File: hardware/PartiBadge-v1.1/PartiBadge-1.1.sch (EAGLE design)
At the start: 23 parts, among them J1 I2C, J2 Supply

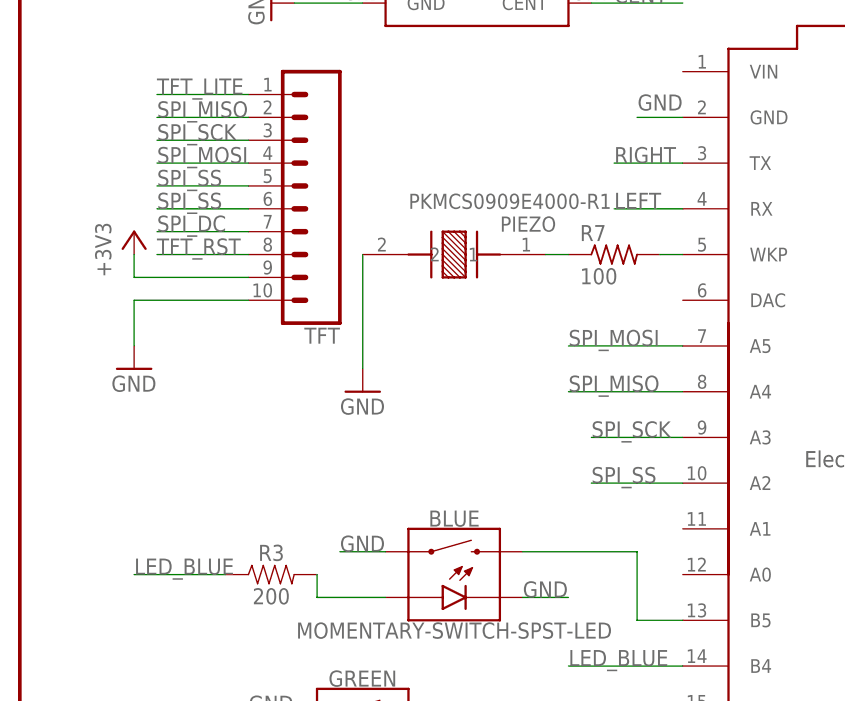
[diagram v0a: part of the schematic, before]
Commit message: moved tft cs pin; closes #50
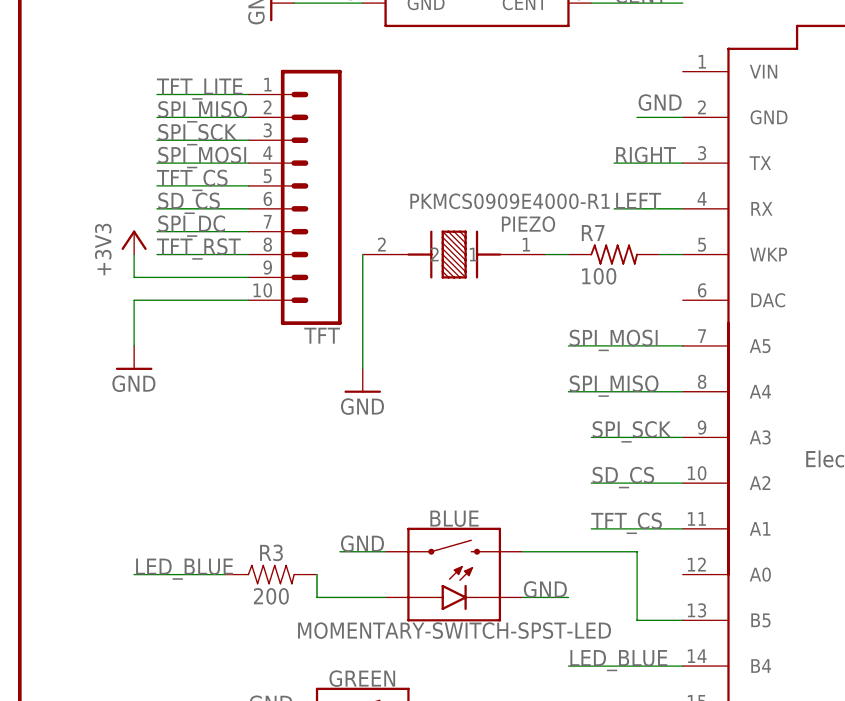
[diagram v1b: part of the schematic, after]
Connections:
- removed net SPI_SS: ELECTRON.A2, TFT.5, TFT.6
- new net SD_CS: ELECTRON.A2, TFT.6
- new net TFT_CS: ELECTRON.A1, TFT.5
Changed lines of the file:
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@@
 </segment>
 </net>
-<net name="SPI_SS" class="0">
+<net name="SD_CS" class="0">
 <segment>
 <pinref part="ELECTRON" gate="G$1" pin="A2"/>
 <wire x1="12.7" y1="48.26" x2="2.54" y2="48.26" width="0.1524" layer="91"/>
 <label x="2.54" y="48.26" size="1.778" layer="95"/>
-</segment>
-<segment>
-<pinref part="TFT" gate="G$1" pin="5"/>
-<wire x1="-35.56" y1="81.28" x2="-45.72" y2="81.28" width="0.1524" layer="91"/>
-<label x="-45.72" y="81.28" size="1.778" layer="95"/>
 </segment>
 <segment>
@@
 </segment>
 </net>
+<net name="TFT_CS" class="0">
+<segment>
+<pinref part="TFT" gate="G$1" pin="5"/>
+<wire x1="-35.56" y1="81.28" x2="-45.72" y2="81.28" width="0.1524" layer="91"/>
+<label x="-45.72" y="81.28" size="1.778" layer="95"/>
+</segment>
+<segment>
+<pinref part="ELECTRON" gate="G$1" pin="A1"/>
+<wire x1="12.7" y1="43.18" x2="2.54" y2="43.18" width="0.1524" layer="91"/>
+<label x="2.54" y="43.18" size="1.778" layer="95"/>
+</segment>
+</net>

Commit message: rev partibadge hardware for ndc oslo
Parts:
- added ETHANOL: (no value), SparkFun-Connectors:CONN_08"
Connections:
- new net RX: ELECTRON.RX, ETHANOL.2
- new net TX: ELECTRON.TX, ETHANOL.3
- net 3V3: now also ETHANOL.8
- net GND: now also ETHANOL.6
- net LEFT: now also ELECTRON.DAC; no longer ELECTRON.RX
- net RIGHT: now also ELECTRON.A0; no longer ELECTRON.TX
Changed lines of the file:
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@@
 </part>
 <part name="R8" library="rcl" library_urn="urn:adsk.eagle:library:334" deviceset="R-US_" device="M0805" package3d_urn="urn:adsk.eagle:package:23556/1" value="100"/>
+<part name="ETHANOL" library="SparkFun-Connectors" library_urn="urn:adsk.eagle:library:513" deviceset="CONN_08" device="&quot;" package3d_urn="urn:adsk.eagle:package:38138/1"/>
+<part name="GND7" library="supply1" library_urn="urn:adsk.eagle:library:371" deviceset="GND" device=""/>
+<part name="+3V7" library="supply1" library_urn="urn:adsk.eagle:library:371" deviceset="+3V3" device=""/>
 </parts>
 <sheets>
@@
 <instance part="PIEZO" gate="G$1" x="-12.7" y="73.66" smashed="yes" rot="R270">
 <attribute name="NAME" x="-7.601059375" y="76.2" size="1.68265" layer="95"/>
-<attribute name="VALUE" x="-17.769109375" y="78.734559375" size="1.679990625" layer="96"/>
+<attribute name="VALUE" x="-22.849109375" y="68.574559375" size="1.679990625" layer="96"/>
 </instance>
 <instance part="S5" gate="1" x="58.42" y="15.24" rot="R180"/>
@@
 <instance part="PARTIFRAME" gate="V" x="86.36" y="-40.64"/>
 <instance part="R8" gate="G$1" x="78.74" y="20.32" rot="R90"/>
+<instance part="ETHANOL" gate="G$1" x="53.34" y="-12.7" rot="R180"/>
+<instance part="GND7" gate="1" x="40.64" y="-17.78" rot="R270"/>
+<instance part="+3V7" gate="G$1" x="40.64" y="-22.86" rot="R90"/>
 </instances>
 <busses>
@@
 <pinref part="GND6" gate="1" pin="GND"/>
 <wire x1="-22.86" y1="101.6" x2="-30.48" y2="101.6" width="0.1524" layer="91"/>
+</segment>
+<segment>
+<pinref part="ETHANOL" gate="G$1" pin="6"/>
+<wire x1="48.26" y1="-17.78" x2="43.18" y2="-17.78" width="0.1524" layer="91"/>
+<pinref part="GND7" gate="1" pin="GND"/>
 </segment>
 </net>
@@
 <wire x1="78.74" y1="25.4" x2="78.74" y2="30.48" width="0.1524" layer="91"/>
 </segment>
+<segment>
+<pinref part="ETHANOL" gate="G$1" pin="8"/>
+<wire x1="48.26" y1="-22.86" x2="43.18" y2="-22.86" width="0.1524" layer="91"/>
+<pinref part="+3V7" gate="G$1" pin="+3V3"/>
+</segment>
 </net>
 <net name="N$4" class="0">
@@
 <segment>
 <pinref part="BLUE" gate="G$1" pin="2"/>
-<wire x1="-5.08" y1="40.64" x2="7.62" y2="40.64" width="0.1524" layer="91"/>
-<wire x1="7.62" y1="40.64" x2="7.62" y2="33.02" width="0.1524" layer="91"/>
+<wire x1="-5.08" y1="40.64" x2="2.54" y2="40.64" width="0.1524" layer="91"/>
+<wire x1="2.54" y1="40.64" x2="2.54" y2="33.02" width="0.1524" layer="91"/>
 <pinref part="ELECTRON" gate="G$1" pin="B5"/>
-<wire x1="7.62" y1="33.02" x2="12.7" y2="33.02" width="0.1524" layer="91"/>
+<wire x1="2.54" y1="33.02" x2="12.7" y2="33.02" width="0.1524" layer="91"/>
 </segment>
 </net>
@@
 </segment>
 <segment>
-<pinref part="ELECTRON" gate="G$1" pin="RX"/>
-<wire x1="12.7" y1="78.74" x2="5.08" y2="78.74" width="0.1524" layer="91"/>
-<label x="5.08" y="78.74" size="1.778" layer="95"/>
+<pinref part="ELECTRON" gate="G$1" pin="DAC"/>
+<wire x1="12.7" y1="68.58" x2="7.62" y2="68.58" width="0.1524" layer="91"/>
+<label x="7.62" y="68.58" size="1.778" layer="95"/>
 </segment>
 </net>
@@
 </segment>
 <segment>
-<pinref part="ELECTRON" gate="G$1" pin="TX"/>
-<wire x1="12.7" y1="83.82" x2="5.08" y2="83.82" width="0.1524" layer="91"/>
-<label x="5.08" y="83.82" size="1.778" layer="95"/>
+<pinref part="ELECTRON" gate="G$1" pin="A0"/>
+<wire x1="12.7" y1="38.1" x2="5.08" y2="38.1" width="0.1524" layer="91"/>
+<label x="5.08" y="38.1" size="1.778" layer="95"/>
 </segment>
 </net>
@@
 </segment>
 </net>
+<net name="RX" class="0">
+<segment>
+<pinref part="ETHANOL" gate="G$1" pin="2"/>
+<wire x1="48.26" y1="-7.62" x2="43.18" y2="-7.62" width="0.1524" layer="91"/>
+<label x="43.18" y="-7.62" size="1.778" layer="95"/>
+</segment>
+<segment>
+<pinref part="ELECTRON" gate="G$1" pin="RX"/>
+<wire x1="12.7" y1="78.74" x2="7.62" y2="78.74" width="0.1524" layer="91"/>
+<label x="7.62" y="78.74" size="1.778" layer="95"/>
+</segment>
+</net>
+<net name="TX" class="0">
+<segment>
+<pinref part="ETHANOL" gate="G$1" pin="3"/>
+<wire x1="48.26" y1="-10.16" x2="43.18" y2="-10.16" width="0.1524" layer="91"/>
+<label x="43.18" y="-10.16" size="1.778" layer="95"/>
+</segment>
+<segment>
+<pinref part="ELECTRON" gate="G$1" pin="TX"/>
+<wire x1="12.7" y1="83.82" x2="7.62" y2="83.82" width="0.1524" layer="91"/>
+<label x="7.62" y="83.82" size="1.778" layer="95"/>
+</segment>
+</net>

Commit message: updated schematic and board
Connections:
- removed net RX: ELECTRON.RX, ETHANOL.2
- removed net TX: ELECTRON.TX, ETHANOL.3
- new net ELECTRON_RX: ELECTRON.RX, ETHANOL.3
- new net ELECTRON_TX: ELECTRON.TX, ETHANOL.2
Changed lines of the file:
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@@
 </segment>
 </net>
-<net name="RX" class="0">
+<net name="ELECTRON_RX" class="0">
+<segment>
+<pinref part="ELECTRON" gate="G$1" pin="RX"/>
+<wire x1="12.7" y1="78.74" x2="-5.08" y2="78.74" width="0.1524" layer="91"/>
+<label x="-5.08" y="78.74" size="1.778" layer="95"/>
+</segment>
+<segment>
+<pinref part="ETHANOL" gate="G$1" pin="3"/>
+<wire x1="48.26" y1="-10.16" x2="30.48" y2="-10.16" width="0.1524" layer="91"/>
+<label x="30.48" y="-10.16" size="1.778" layer="95"/>
+</segment>
+</net>
+<net name="ELECTRON_TX" class="0">
+<segment>
+<pinref part="ELECTRON" gate="G$1" pin="TX"/>
+<wire x1="12.7" y1="83.82" x2="-5.08" y2="83.82" width="0.1524" layer="91"/>
+<label x="-5.08" y="83.82" size="1.778" layer="95"/>
+</segment>
 <segment>
 <pinref part="ETHANOL" gate="G$1" pin="2"/>
-<wire x1="48.26" y1="-7.62" x2="43.18" y2="-7.62" width="0.1524" layer="91"/>
-<label x="43.18" y="-7.62" size="1.778" layer="95"/>
-</segment>
-<segment>
-<pinref part="ELECTRON" gate="G$1" pin="RX"/>
-<wire x1="12.7" y1="78.74" x2="7.62" y2="78.74" width="0.1524" layer="91"/>
-<label x="7.62" y="78.74" size="1.778" layer="95"/>
+<wire x1="48.26" y1="-7.62" x2="30.48" y2="-7.62" width="0.1524" layer="91"/>
+<label x="30.48" y="-7.62" size="1.778" layer="95"/>
 </segment>
 </net>
-<net name="TX" class="0">
-<segment>
-<pinref part="ETHANOL" gate="G$1" pin="3"/>
-<wire x1="48.26" y1="-10.16" x2="43.18" y2="-10.16" width="0.1524" layer="91"/>
-<label x="43.18" y="-10.16" size="1.778" layer="95"/>
-</segment>
-<segment>
-<pinref part="ELECTRON" gate="G$1" pin="TX"/>
-<wire x1="12.7" y1="83.82" x2="7.62" y2="83.82" width="0.1524" layer="91"/>
-<label x="7.62" y="83.82" size="1.778" layer="95"/>
-</segment>
-</net>
